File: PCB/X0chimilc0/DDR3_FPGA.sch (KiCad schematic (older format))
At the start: 1 part

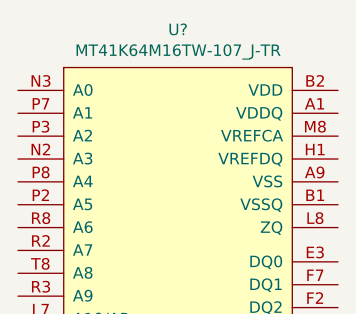
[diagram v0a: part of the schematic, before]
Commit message: Component PDFs
added relevant PDF datasheets and some minor schematic edits
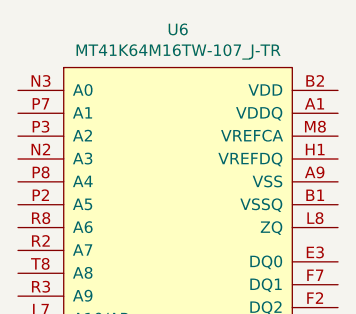
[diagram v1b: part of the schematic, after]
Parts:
- gave numbers to parts that had none: 1
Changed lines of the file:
@@
 $EndDescr
 $Comp
-L AVR-KiCAD-Lib-ICs:MT41K64M16TW-107_J-TR U?
+L AVR-KiCAD-Lib-ICs:MT41K64M16TW-107_J-TR U6
 U 1 1 5DE49E54
 P 5550 1750
-F 0 "U?" H 6050 2165 50  0000 C CNN
+F 0 "U6" H 6050 2165 50  0000 C CNN
 F 1 "MT41K64M16TW-107_J-TR" H 5750 2150 50  0001 C CNN
 F 2 "AVR-KiCAD-Lib-ICs:MT41K64M16TW_107_J_TR" H 5350 1950 50  0001 C CNN

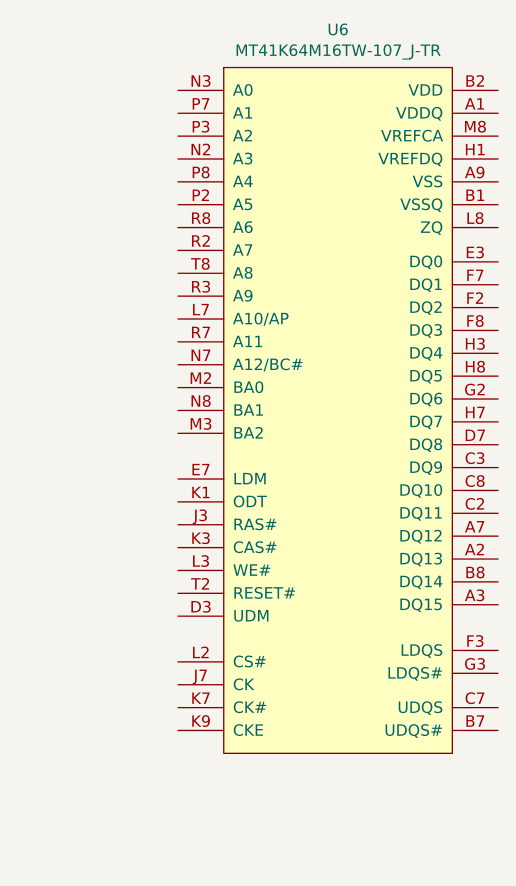
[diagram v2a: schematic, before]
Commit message: USB
USB C page of schematics first pass complete
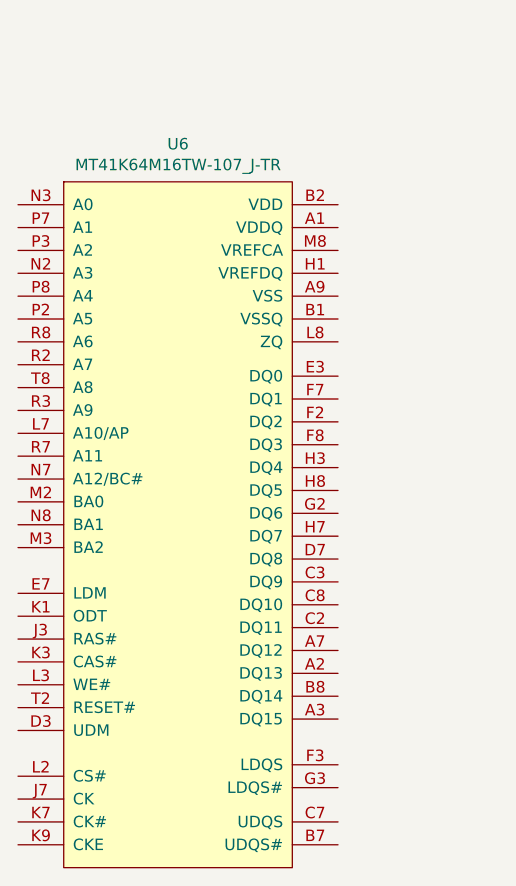
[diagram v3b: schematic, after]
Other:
- moved on the sheet: U6
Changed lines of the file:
@@
 $Descr A4 11693 8268
 encoding utf-8
-Sheet 6 8
+Sheet 6 10
 Title ""
 Date ""
@@
 L AVR-KiCAD-Lib-ICs:MT41K64M16TW-107_J-TR U6
 U 1 1 5DE49E54
-P 5550 1750
-F 0 "U6" H 6050 2165 50  0000 C CNN
-F 1 "MT41K64M16TW-107_J-TR" H 5750 2150 50  0001 C CNN
-F 2 "AVR-KiCAD-Lib-ICs:MT41K64M16TW_107_J_TR" H 5350 1950 50  0001 C CNN
-F 3 "http://www.micron.com/~/media/documents/products/data-sheet/dram/ddr3/1gb_1_35v_ddr3l.pdf" H 5600 2050 50  0001 C CNN
-F 4 "4.29000" H 5800 2200 50  0001 C CNN "Cost QTY: 1"
-F 5 "3.09830" H 5900 2300 50  0001 C CNN "Cost QTY: 1000"
-F 6 "*" H 6000 2400 50  0001 C CNN "Cost QTY: 2500"
-F 7 "*" H 6100 2500 50  0001 C CNN "Cost QTY: 5000"
-F 8 "*" H 6200 2600 50  0001 C CNN "Cost QTY: 10000"
-F 9 "Micron Technology Inc." H 6300 2700 50  0001 C CNN "MFR"
-F 10 "MT41K64M16TW-107:J TR" H 6400 2800 50  0001 C CNN "MFR#"
-F 11 "Digikey" H 6500 2900 50  0001 C CNN "Vendor"
-F 12 "557-2010-1-ND" H 6600 3000 50  0001 C CNN "Vendor #"
-F 13 "AVR" H 6700 3100 50  0001 C CNN "Designer"
-F 14 "1.2mm" H 6800 3200 50  0001 C CNN "Height"
-F 15 "12/1/2019" H 7900 4300 50  0001 C CNN "Date Created"
-F 16 "12/1/2019" H 6900 3300 50  0001 C CNN "Date Modified"
-F 17 "Yes" H 7000 3400 50  0001 C CNN "Lead-Free ?"
-F 18 "1" H 7100 3500 50  0001 C CNN "RoHS Levels"
-F 19 "SMT" H 7200 3600 50  0001 C CNN "Mounting"
-F 20 "96" H 7300 3700 50  0001 C CNN "Pin Count #"
-F 21 "Active" H 7400 3800 50  0001 C CNN "Status"
-F 22 "*" H 7500 3900 50  0001 C CNN "Tolerance"
-F 23 "SDRAM-DDR3L" H 7600 4000 50  0001 C CNN "Type"
-F 24 "1.283V ~ 1.45V" H 7700 4100 50  0001 C CNN "Voltage"
-F 25 "BGA96" H 7800 4250 50  0001 C CNN "Package"
-F 26 "SDRAM - DDR3L Memory IC 1Gb (64M x 16) Parallel 933MHz 20ns 96-FBGA (8x14)" H 8100 4550 50  0001 C CNN "Description"
-F 27 "MT41K64M16TW-107_J-TR" H 6050 2074 50  0000 C CNN "_Value_"
-F 28 "*" H 8100 4550 50  0001 C CNN "Management_ID"
-	1    5550 1750
+P 4850 2250
+F 0 "U6" H 5350 2665 50  0000 C CNN
+F 1 "MT41K64M16TW-107_J-TR" H 5050 2650 50  0001 C CNN
+F 2 "AVR-KiCAD-Lib-ICs:MT41K64M16TW_107_J_TR" H 4650 2450 50  0001 C CNN
+F 3 "http://www.micron.com/~/media/documents/products/data-sheet/dram/ddr3/1gb_1_35v_ddr3l.pdf" H 4900 2550 50  0001 C CNN
+F 4 "4.29000" H 5100 2700 50  0001 C CNN "Cost QTY: 1"
+F 5 "3.09830" H 5200 2800 50  0001 C CNN "Cost QTY: 1000"
+F 6 "*" H 5300 2900 50  0001 C CNN "Cost QTY: 2500"
+F 7 "*" H 5400 3000 50  0001 C CNN "Cost QTY: 5000"
+F 8 "*" H 5500 3100 50  0001 C CNN "Cost QTY: 10000"
+F 9 "Micron Technology Inc." H 5600 3200 50  0001 C CNN "MFR"
+F 10 "MT41K64M16TW-107:J TR" H 5700 3300 50  0001 C CNN "MFR#"
+F 11 "Digikey" H 5800 3400 50  0001 C CNN "Vendor"
+F 12 "557-2010-1-ND" H 5900 3500 50  0001 C CNN "Vendor #"
+F 13 "AVR" H 6000 3600 50  0001 C CNN "Designer"
+F 14 "1.2mm" H 6100 3700 50  0001 C CNN "Height"
+F 15 "12/1/2019" H 7200 4800 50  0001 C CNN "Date Created"
+F 16 "12/1/2019" H 6200 3800 50  0001 C CNN "Date Modified"
+F 17 "Yes" H 6300 3900 50  0001 C CNN "Lead-Free ?"
+F 18 "1" H 6400 4000 50  0001 C CNN "RoHS Levels"
+F 19 "SMT" H 6500 4100 50  0001 C CNN "Mounting"
+F 20 "96" H 6600 4200 50  0001 C CNN "Pin Count #"
+F 21 "Active" H 6700 4300 50  0001 C CNN "Status"
+F 22 "*" H 6800 4400 50  0001 C CNN "Tolerance"
+F 23 "SDRAM-DDR3L" H 6900 4500 50  0001 C CNN "Type"
+F 24 "1.283V ~ 1.45V" H 7000 4600 50  0001 C CNN "Voltage"
+F 25 "BGA96" H 7100 4750 50  0001 C CNN "Package"
+F 26 "SDRAM - DDR3L Memory IC 1Gb (64M x 16) Parallel 933MHz 20ns 96-FBGA (8x14)" H 7400 5050 50  0001 C CNN "Description"
+F 27 "MT41K64M16TW-107_J-TR" H 5350 2574 50  0000 C CNN "_Value_"
+F 28 "*" H 7400 5050 50  0001 C CNN "Management_ID"
+	1    4850 2250
 	1    0    0    -1
 $EndComp

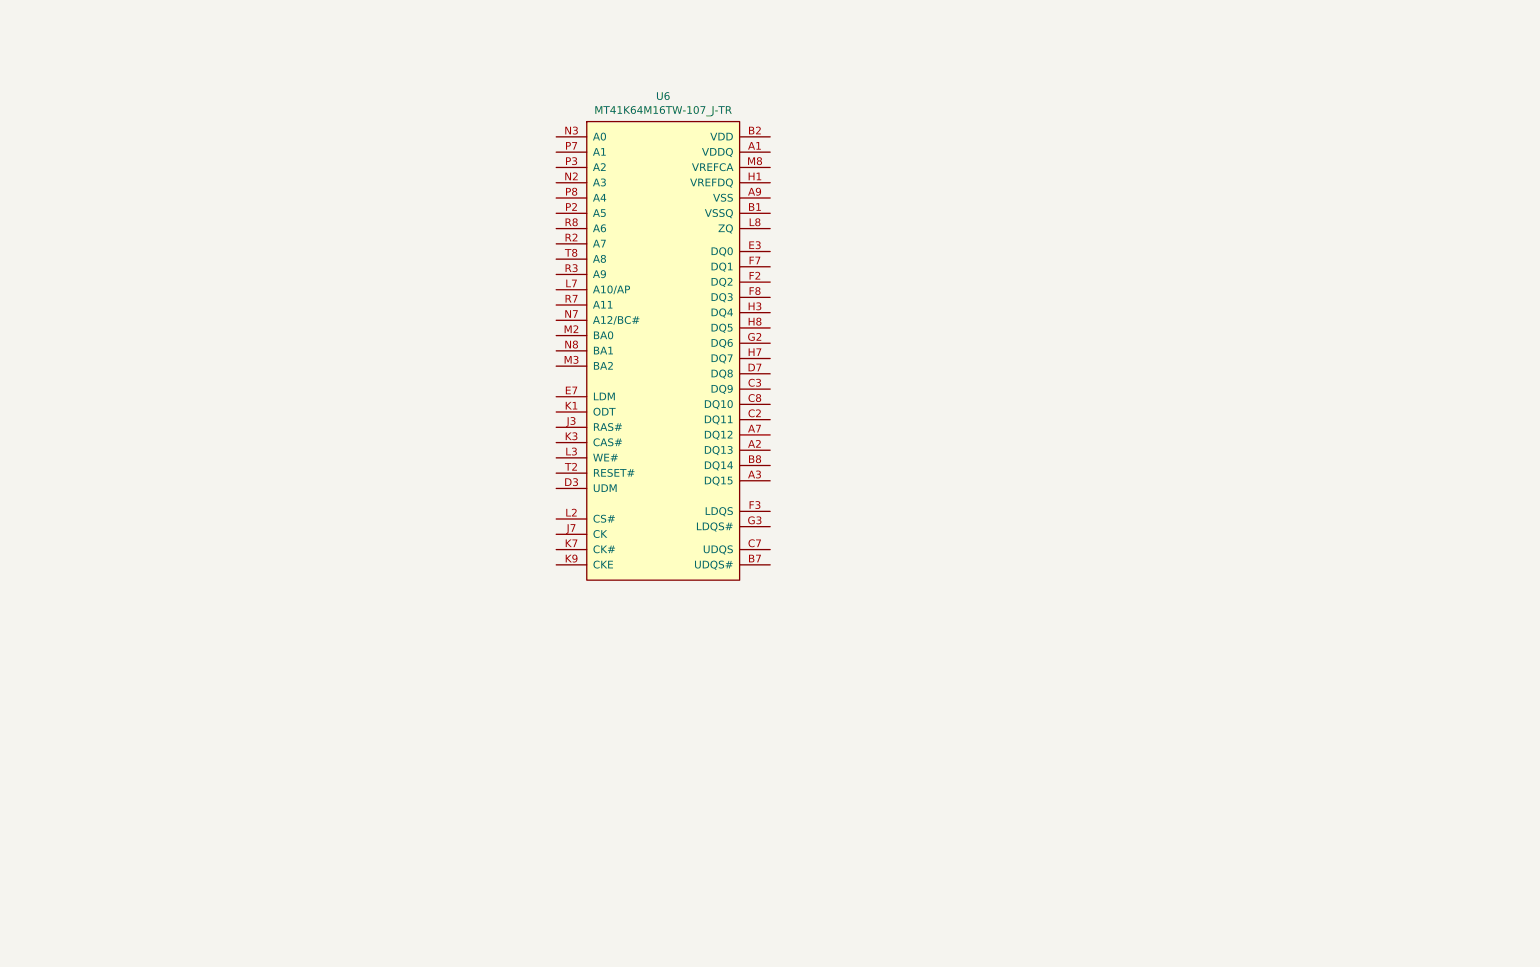
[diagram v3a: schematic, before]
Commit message: DDR3L
Memory schematic for FPGA cloned from OrangeCrab R1.0 schematic, MCU memory started. Both need finishing.
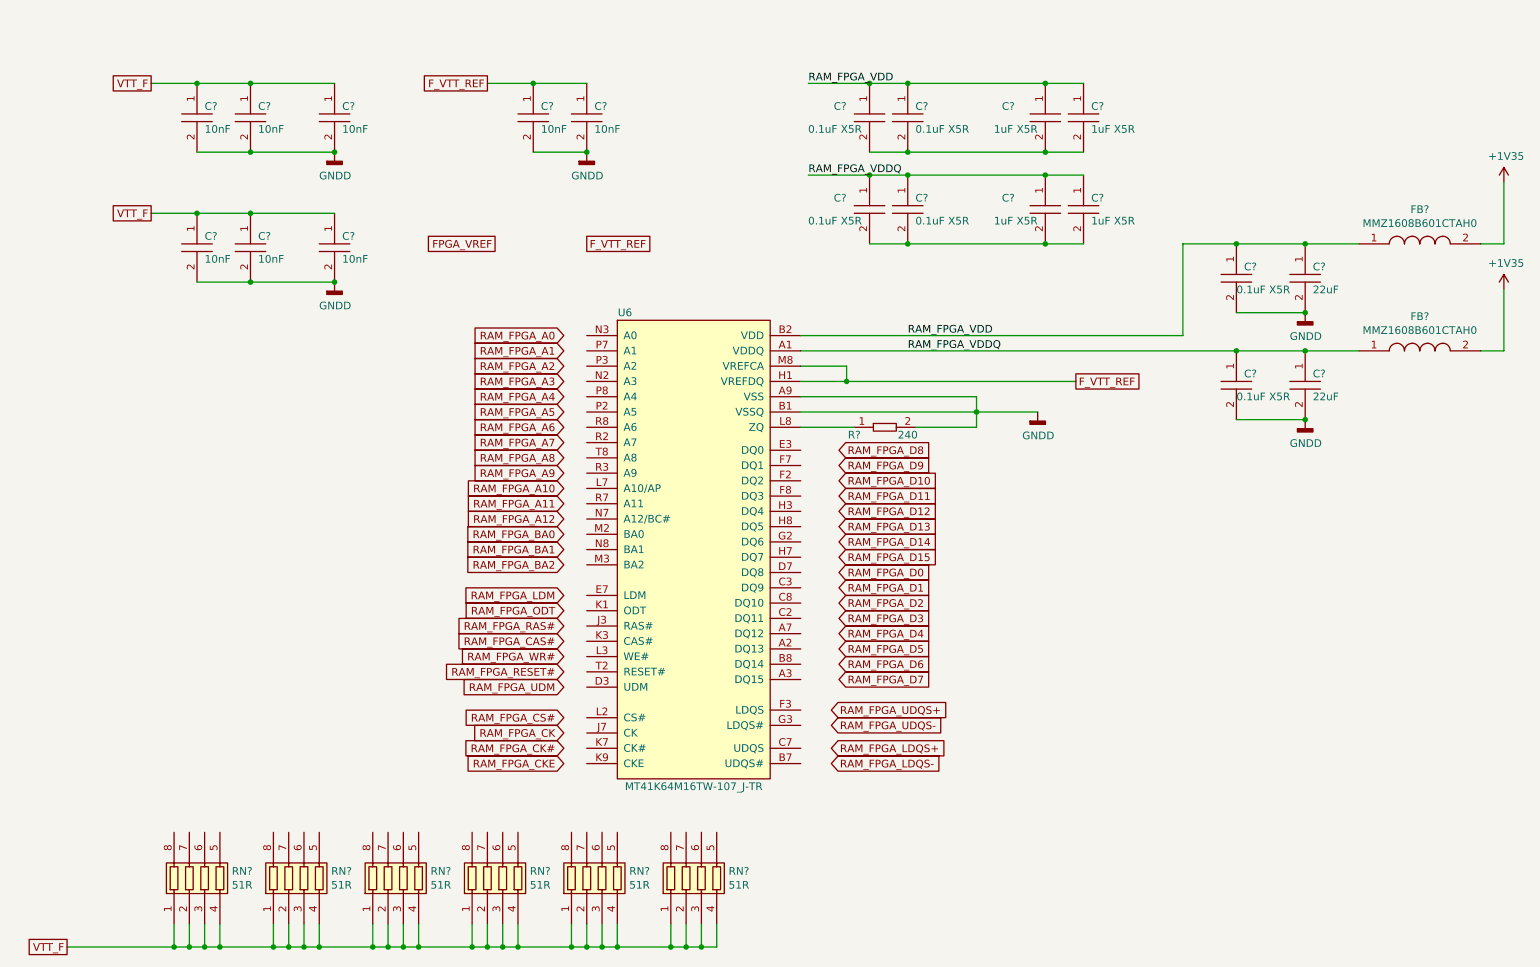
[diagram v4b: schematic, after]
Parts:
- added C? (x6): C0402C104K9PACTU, AVR-KiCAD-Lib-Resistors:R0402, symbol AVR-KiCAD-Lib-Capacitors:C0402C104K9PACTU
- added C? (x4): CC0603KRX5R7BB105, AVR-KiCAD-Lib-Capacitors:C0603, symbol AVR-KiCAD-Lib-Capacitors:CC0603KRX5R7BB105
- added C? (x2): GRM188R60J226MEA0D, AVR-KiCAD-Lib-Capacitors:C0603, symbol AVR-KiCAD-Lib-Capacitors:GRM188R60J226MEA0D
- added C? (x8): C0603X103K1RAC3316, AVR-KiCAD-Lib-Capacitors:C0603, symbol AVR-KiCAD-Lib-Capacitors:C0603X103K1RAC3316
- added FB? (x2): MMZ1608B601CTAH0, AVR-KiCAD-Lib-Resistors:R0603, symbol AVR-KiCAD-Lib-Inductors:MMZ1608B601CTAH0
- added R?: RC0402FR-07240RL, AVR-KiCAD-Lib-Resistors:R0402, symbol AVR-KiCAD-Lib-Resistors:RC0402FR-07240RL
- added RN? (x6): YC124-JR-0751RL, AVR-KiCAD-Lib-Resistors:RN0804, symbol AVR-KiCAD-Lib-Resistors:YC124-JR-0751RL
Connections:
- net RAM_FPGA_VDDQ: now reaches U6.A1 (VDDQ)
- net RAM_FPGA_VDDQ: now also C?.1, C?.1, C?.1, C?.1, C?.1, C?.1, FB?.1
- net GNDD: now reaches U6.A9 (VSS)
- net GNDD: now also U6.B1 (VSSQ), C?.2, C?.2, C?.2, C?.2, C?.2, C?.2, C?.2, C?.2, C?.2, C?.2, C?.2, C?.2, R?.2
- net RAM_FPGA_VDD: now reaches U6.B2 (VDD)
- net RAM_FPGA_VDD: now also C?.1, C?.1, C?.1, C?.1, C?.1, C?.1, FB?.1
- net F_VTT_REF: now reaches U6.H1 (VREFDQ)
- net F_VTT_REF: now also U6.M8 (VREFCA), C?.1, C?.1
- net at U6.L8 (ZQ): now also R?.1
- new net: C?.2, C?.2, C?.2, C?.2 (x2)
- new net +1V35: FB?.2, FB?.2
- new net VTT_F: C?.1, C?.1, C?.1, C?.1, C?.1, C?.1, RN?.1, RN?.1, RN?.1, RN?.1, RN?.1, RN?.1, RN?.2, RN?.2, RN?.2, RN?.2, RN?.2, RN?.2, RN?.3, RN?.3, RN?.3, RN?.3, RN?.3, RN?.3, RN?.4, RN?.4, RN?.4, RN?.4, RN?.4, RN?.4
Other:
- moved on the sheet: U6
